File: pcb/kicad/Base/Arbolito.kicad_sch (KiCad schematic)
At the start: 68 parts, among them J1 Battery, J10 Conn_01x01, J11 Conn_01x01, J12 Conn_01x01, J13 Conn_01x01, J14 Conn_01x01, J2 Conn_01x06_Female, J3 Conn_01x01, J4 Conn_01x01, J5 Conn_01x01, J6 Conn_01x01, J7 Conn_01x01, J8 Conn_01x01, J9 Conn_01x01, P1 USB_C_Plug_USB2.0, Q1 S8050, Q2 S8050, Q3 S8050, SW1 SW_DP3T, SW2 SW_Push, SW3 SW_Push, SW4 SW_Push, U1 NCP115AMX120TCG, U2 CH340C, U3 AP63205WU, U4 ESP-12F, U5 SHT31-DIS

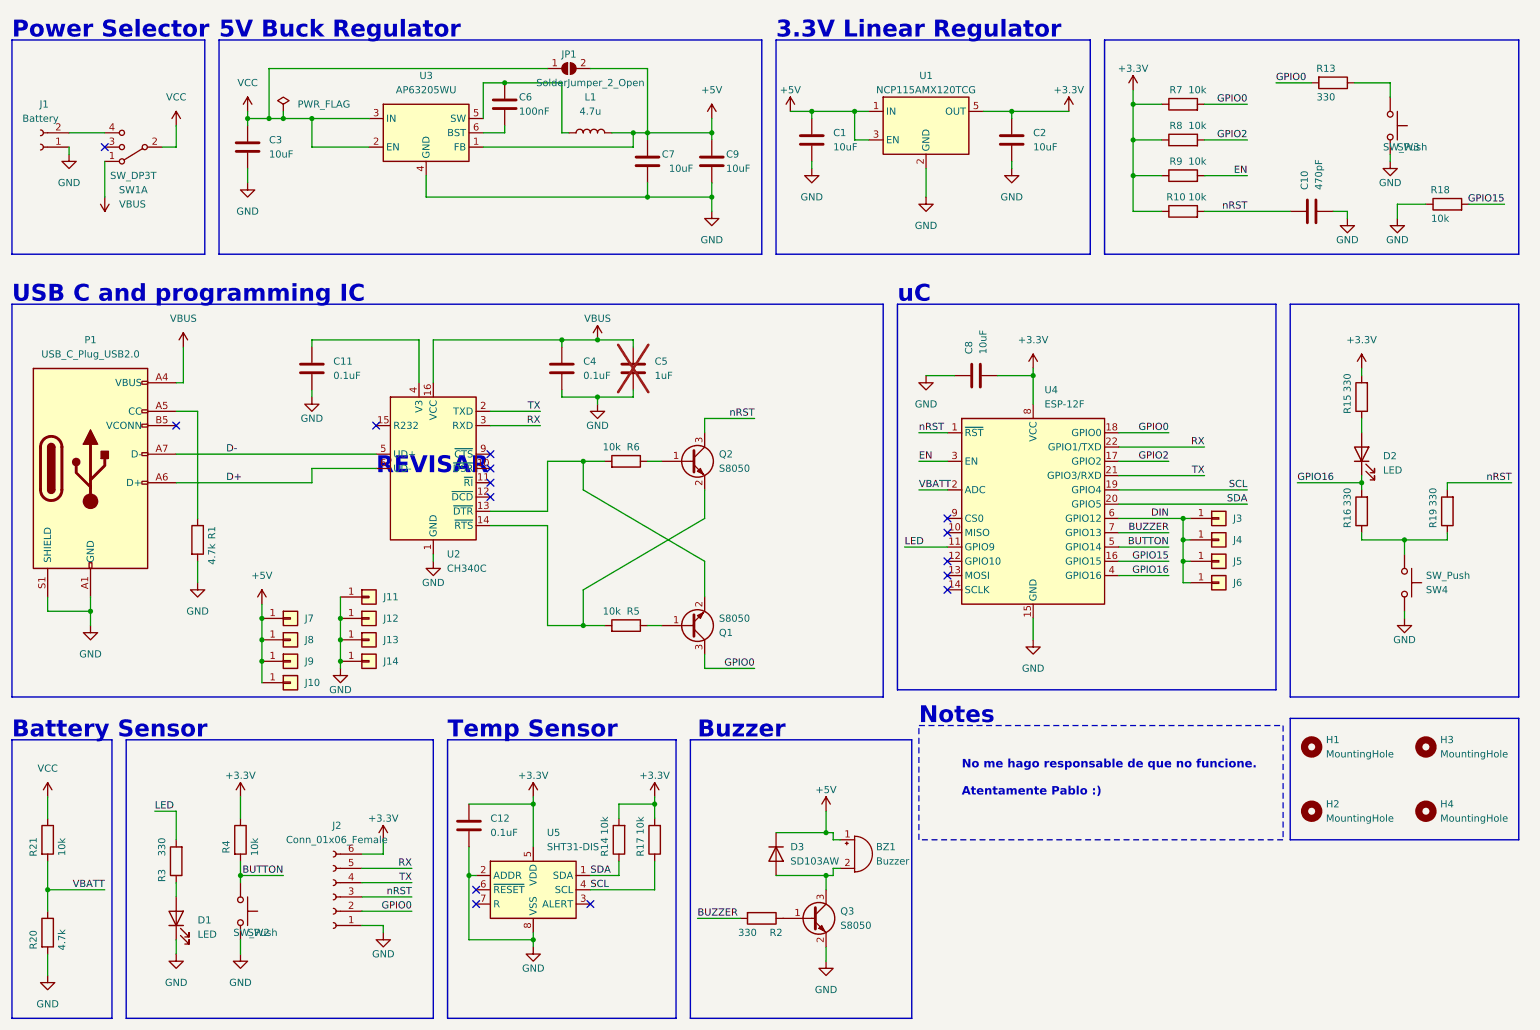
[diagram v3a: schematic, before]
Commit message: Modified USB-C with 3 cents version
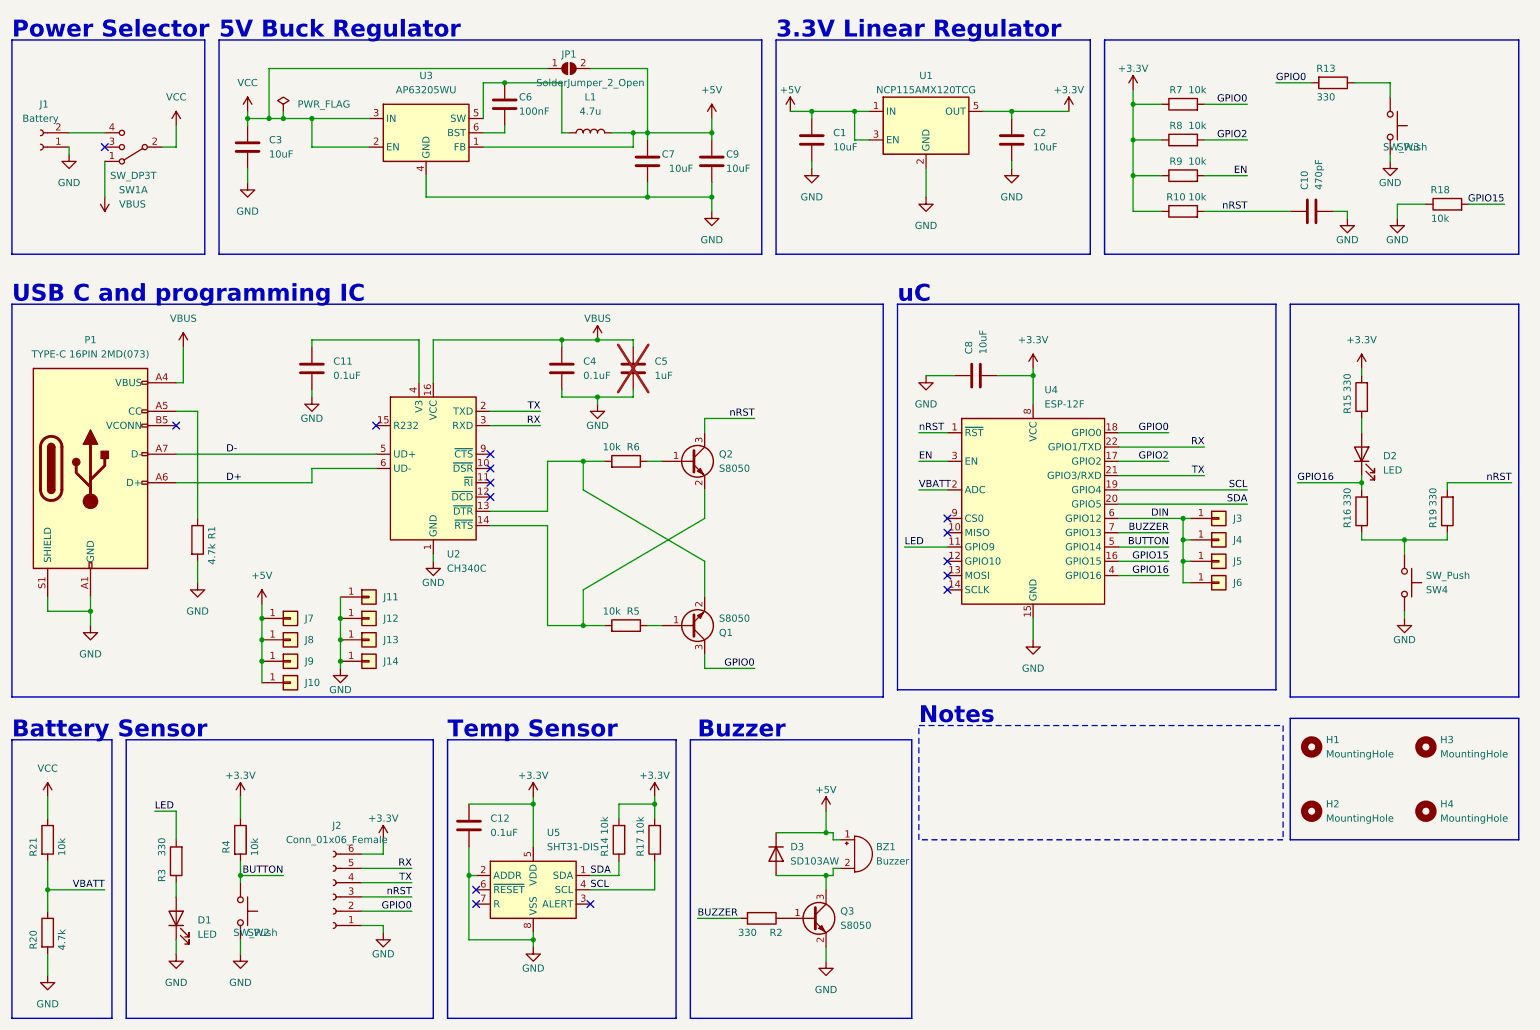
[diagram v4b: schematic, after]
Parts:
- P1: value USB_C_Plug_USB2.0 -> TYPE-C 16PIN 2MD(073); footprint Library:USB C Molex -> Library:TYPE-C 16PIN 2MD(073)
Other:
- note removed: "No me hago responsable de que no funcione. Atentamente Pablo :)"
- note removed: "REVISAR"
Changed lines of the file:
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@@
-    (effects (font (face "Montserrat") (size 3 3) (thickness 0.6) bold (color 0 156 163 1)) (justify left bottom))
-  )
-  (text "REVISAR" (at 80.01 99.06 0)
     (effects (font (face "Montserrat") (size 3 3) (thickness 0.6) bold (color 0 156 163 1)) (justify left bottom))
   )
   (text "5V Buck Regulator" (at 52.07 21.59 0)
     (effects (font (face "Montserrat") (size 3 3) (thickness 0.6) bold (color 0 156 163 1)) (justify left bottom))
-  )
-  (text "No me hago responsable de que no funcione.\n\nAtentamente Pablo :)"
-    (at 184.15 156.21 0)
-    (effects (font (size 1.5 1.5) (thickness 0.2508) bold (color 255 255 255 1)) (justify left bottom))
   )
   (text "Notes" (at 176.53 143.51 0)
@@
       (effects (font (size 1.27 1.27)))
     )
-    (property "Value" "USB_C_Plug_USB2.0" (at 29.21 77.47 0)
-      (effects (font (size 1.27 1.27)))
-    )
-    (property "Footprint" "Library:USB C Molex" (at 33.02 97.79 0)
-      (effects (font (size 1.27 1.27)) hide)
-    )
+    (property "Value" "TYPE-C 16PIN 2MD(073)" (at 29.21 77.47 0)
+      (effects (font (size 1.27 1.27)))
+    )
+    (property "Footprint" "Library:TYPE-C 16PIN 2MD(073)" (at 33.02 97.79 0)
+      (effects (font (size 1.27 1.27)) hide)
+    )

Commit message: idk
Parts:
- C11, C4: value 0.1uF -> 100n
- C12: value 0.1uF -> 100n; now not fitted
- R14, R17, U5: now not fitted
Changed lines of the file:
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@@
   )
   (symbol (lib_id "Sensor_Humidity:SHT31-DIS") (at 107.95 172.72 0) (unit 1)
-    (in_bom yes) (on_board yes) (dnp no) (fields_autoplaced)
+    (in_bom yes) (on_board yes) (dnp yes) (fields_autoplaced)
     (property "Reference" "U5" (at 110.3756 162.56 0)
       (effects (font (size 1.27 1.27)) (justify left))
@@
     )
     (property "Datasheet" "https://www.sensirion.com/fileadmin/user_upload/customers/sensirion/Dokumente/2_Humidity_Sensors/Datasheets/Sensirion_Humidity_Sensors_SHT3x_Datasheet_digital.pdf" (at 107.95 171.45 0)
+      (effects (font (size 1.27 1.27)) hide)
+    )
+    (property "dnp" "" (at 107.95 172.72 0)
+      (effects (font (size 1.27 1.27)) hide)
+    )
+    (property "Field5" "" (at 107.95 172.72 0)
       (effects (font (size 1.27 1.27)) hide)
     )
@@
   )
   (symbol (lib_id "Device:C") (at 96.52 161.29 0) (unit 1)
-    (in_bom yes) (on_board yes) (dnp no) (fields_autoplaced)
+    (in_bom yes) (on_board yes) (dnp yes) (fields_autoplaced)
     (property "Reference" "C12" (at 100.33 160.0199 0)
       (effects (font (size 1.27 1.27)) (justify left))
     )
-    (property "Value" "0.1uF" (at 100.33 162.5599 0)
+    (property "Value" "100n" (at 100.33 162.5599 0)
       (effects (font (size 1.27 1.27)) (justify left))
     )
@@
       (effects (font (size 1.27 1.27)) (justify left))
     )
-    (property "Value" "0.1uF" (at 72.39 81.2799 0)
+    (property "Value" "100n" (at 72.39 81.2799 0)
       (effects (font (size 1.27 1.27)) (justify left))
     )
@@
   )
   (symbol (lib_id "Device:R") (at 123.19 163.83 180) (unit 1)
-    (in_bom yes) (on_board yes) (dnp no)
+    (in_bom yes) (on_board yes) (dnp yes)
     (property "Reference" "R14" (at 120.65 165.1 90)
       (effects (font (size 1.27 1.27)))
@@
       (effects (font (size 1.27 1.27)) (justify left))
     )
-    (property "Value" "0.1uF" (at 116.84 81.2799 0)
+    (property "Value" "100n" (at 116.84 81.2799 0)
       (effects (font (size 1.27 1.27)) (justify left))
     )
@@
   )
   (symbol (lib_id "Device:R") (at 129.54 163.83 180) (unit 1)
-    (in_bom yes) (on_board yes) (dnp no)
+    (in_bom yes) (on_board yes) (dnp yes)
     (property "Reference" "R17" (at 127 165.1 90)
       (effects (font (size 1.27 1.27)))
